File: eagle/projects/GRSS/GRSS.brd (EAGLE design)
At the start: 85 x 47 mm, 32 parts, among them J1 MOL-SL-2-RA, J10 MOL-SL-2-RA, J11 M02PTH, J2 MOL-SL-2-RA, J3 MOL-SL-2-RA, J4 MOL-SL-2-RA, J5 MOL-SL-2-RA, J6 MOL-SL-2-RA, J7 MOL-SL-2-RA, J8 MOL-SL-2-RA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

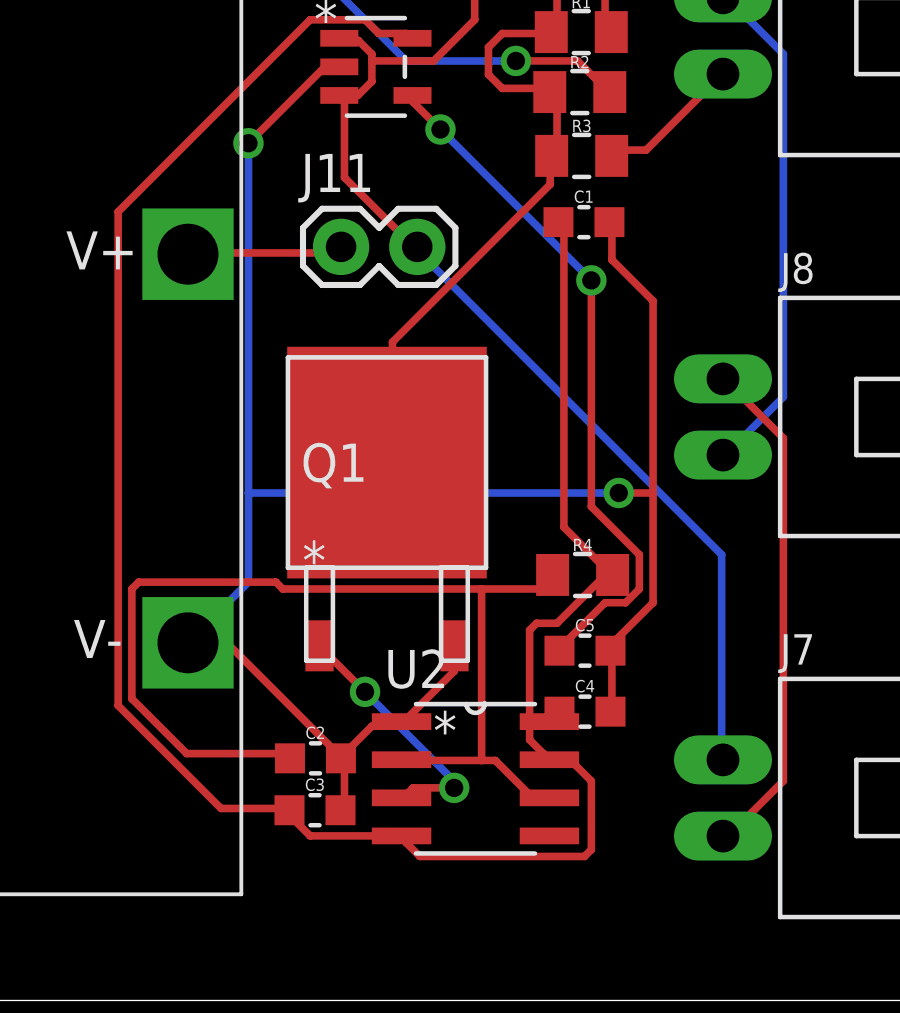
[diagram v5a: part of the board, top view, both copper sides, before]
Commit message: A few 0805 caps added to lib and now GRSS jelly bean all 0805 (just did caps)
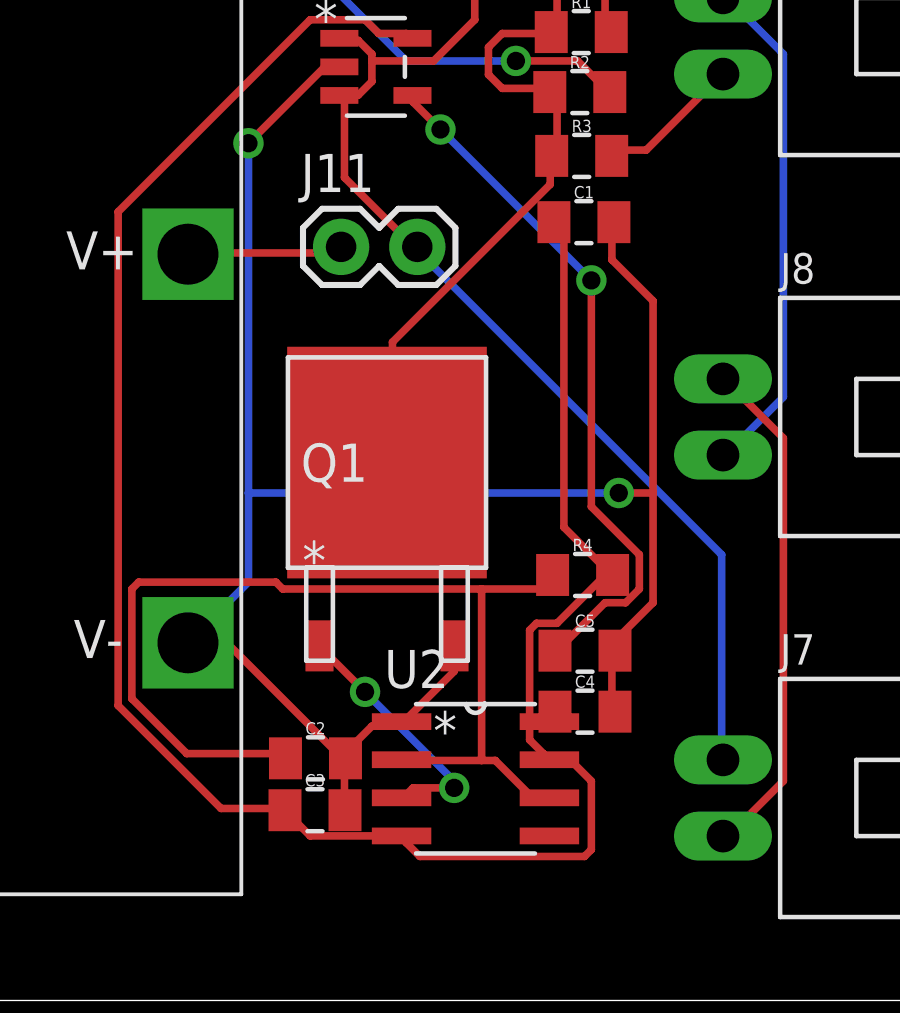
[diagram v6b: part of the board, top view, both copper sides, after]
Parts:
- C1, C2, C3, C4, C5: device grss:C0603 -> grss:C0805

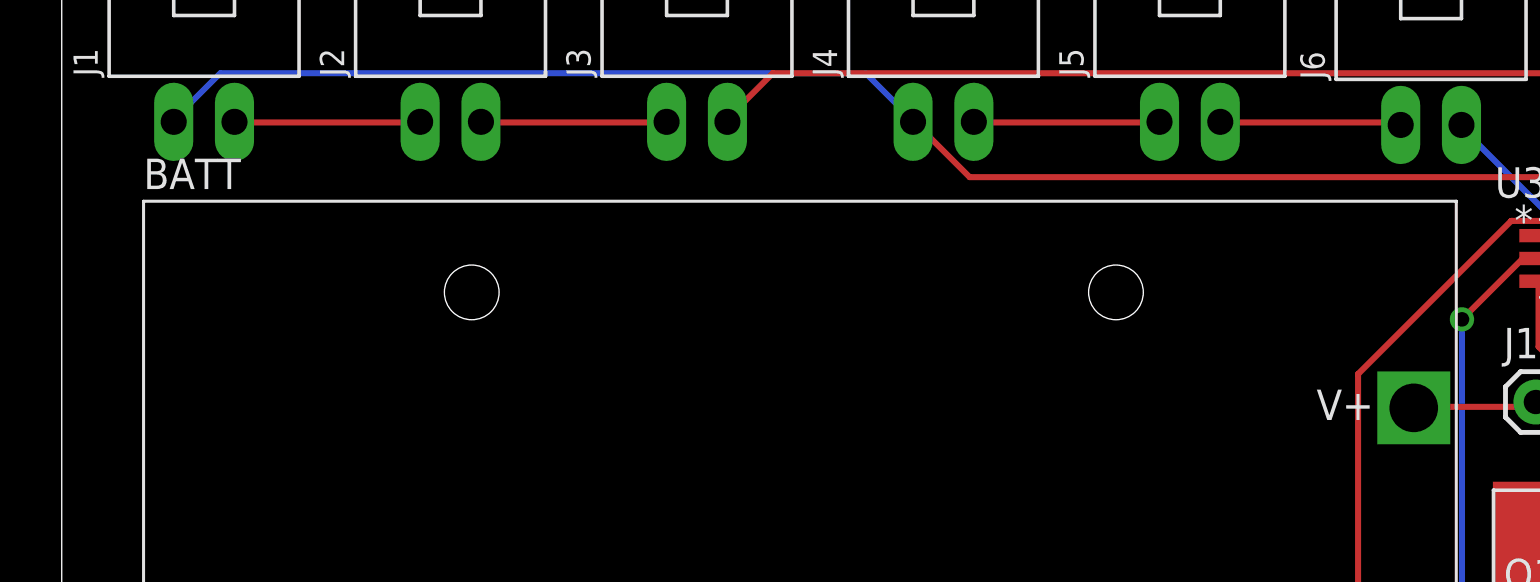
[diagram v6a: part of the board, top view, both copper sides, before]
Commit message: battery holder pn update
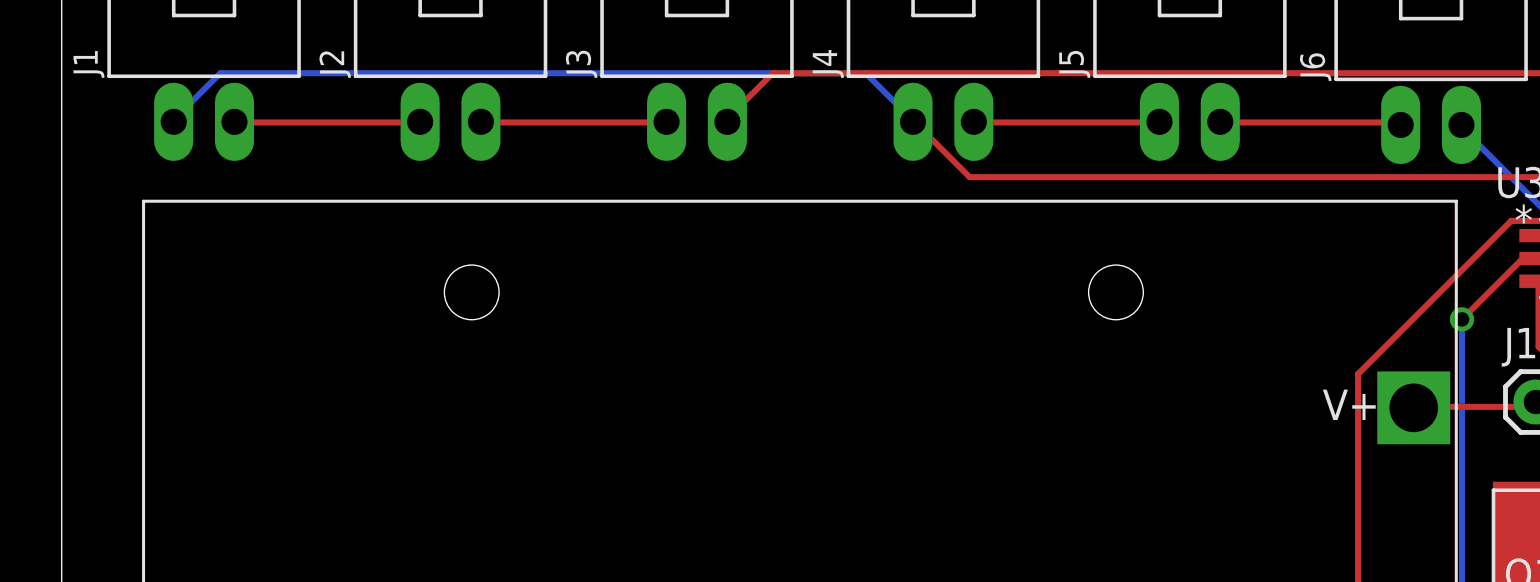
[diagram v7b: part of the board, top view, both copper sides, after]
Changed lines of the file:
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@@
 <elements>
 <element name="BATT" library="grss" package="BC9VPC" value="9V" x="3.42" y="3.54">
-<attribute name="VENDOR_PN" value="BC9VPC-ND" x="3.42" y="3.54" size="1.778" layer="27" display="off"/>
+<attribute name="VENDOR_PN" value="BH9V-PC-ND" x="3.42" y="3.54" size="1.778" layer="27" display="off"/>
 <attribute name="VENDOR" value="Digi-key" x="3.42" y="3.54" size="1.778" layer="27" display="off"/>
-<attribute name="MANUFACTURER" value="MPD (Memory Protection Devices)" x="3.42" y="3.54" size="1.778" layer="27" display="off"/>
-<attribute name="MANUFACTURER_PN" value="BC9VPC" x="3.42" y="3.54" size="1.778" layer="27" display="off"/>
+<attribute name="MANUFACTURER" value="MPD" x="3.42" y="3.54" size="1.778" layer="27" display="off"/>
+<attribute name="MANUFACTURER_PN" value="BH9VPC" x="3.42" y="3.54" size="1.778" layer="27" display="off"/>
+<attribute name="PROD_ID" value="BATT-10855" x="3.42" y="3.54" size="1.778" layer="27" display="off"/>
 </element>
 <element name="C1" library="grss" package="C0805" value="100nF" x="69.704" y="25.944">

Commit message: TP on GND
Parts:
- added TP4: (no value), grss:TP10R
- C1: value 100nF -> 0.1uF
- C5: value 10pF -> 0.01uF
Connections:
- net GND: now also TP4.TP
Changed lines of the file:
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@@
 <attribute name="PROD_ID" value="BATT-10855" x="3.42" y="3.54" size="1.778" layer="27" display="off"/>
 </element>
-<element name="C1" library="grss" package="C0805" value="100nF" x="69.704" y="25.944">
+<element name="C1" library="grss" package="C0805" value="0.1uF" x="69.704" y="25.944">
 <attribute name="VENDOR_PN" value="490-1683-1-ND" x="69.704" y="25.944" size="1.778" layer="27" display="off"/>
 <attribute name="VENDOR" value="Digi-key" x="69.704" y="25.944" size="1.778" layer="27" display="off"/>
@@
 <attribute name="TOLERANCE" value="10%" x="69.74" y="9.628" size="1.778" layer="27" display="off"/>
 </element>
-<element name="C5" library="grss" package="C0805" value="10pF" x="69.74" y="11.66">
-<attribute name="VENDOR_PN" value="490-5530-1-ND" x="69.74" y="11.66" size="1.778" layer="27" display="off"/>
+<element name="C5" library="grss" package="C0805" value="0.01uF" x="69.74" y="11.66">
+<attribute name="VENDOR_PN" value="490-9742-1-ND" x="69.74" y="11.66" size="1.778" layer="27" display="off"/>
 <attribute name="VENDOR" value="Digi-key" x="69.74" y="11.66" size="1.778" layer="27" display="off"/>
 <attribute name="MANUFACTURER" value="Murata" x="69.74" y="11.66" size="1.778" layer="27" display="off"/>
-<attribute name="VOLTAGE" value="250V" x="69.74" y="11.66" size="1.778" layer="27" display="off"/>
-<attribute name="MANUFACTURER_PN" value="GRM21A5C2E100JW01D" x="69.74" y="11.66" size="1.778" layer="27" display="off"/>
-<attribute name="TEMP_COEFF" value="C0G, NP0" x="69.74" y="11.66" size="1.778" layer="27" display="off"/>
+<attribute name="VOLTAGE" value="50V" x="69.74" y="11.66" size="1.778" layer="27" display="off"/>
+<attribute name="MANUFACTURER_PN" value="GRM216R71H103JA01D" x="69.74" y="11.66" size="1.778" layer="27" display="off"/>
+<attribute name="TEMP_COEFF" value="X7R" x="69.74" y="11.66" size="1.778" layer="27" display="off"/>
 <attribute name="TOLERANCE" value="5%" x="69.74" y="11.66" size="1.778" layer="27" display="off"/>
 </element>
@@
 <attribute name="MANUFACTURER_PN" value="ERJ-P06F4701V" x="-6" y="-34" size="1.778" layer="27" display="off"/>
 <attribute name="VENDOR_PN" value="P16073CT-ND" x="-6" y="-34" size="1.778" layer="27" display="off"/>
+</element>
+<element name="TP4" library="grss" package="TP10R" value="" x="-5" y="-39">
+<attribute name="TP_SIGNAL_NAME" value="" x="-5" y="-39" size="1.778" layer="27" display="off"/>
 </element>
 </elements>
@@
 <via x="70.866" y="16.9164" extent="1-16" drill="0.6096"/>
 <contactref element="R5" pad="1"/>
+<contactref element="TP4" pad="TP"/>
 <wire x1="-7" y1="-34" x2="56.506" y2="11.922" width="0" layer="19" extent="1-16"/>
+<wire x1="-5" y1="-39" x2="-7" y2="-34" width="0" layer="19" extent="1-1"/>
 </signal>
 <signal name="THRTRIG">
